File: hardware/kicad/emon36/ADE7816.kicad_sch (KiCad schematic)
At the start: 42 parts, among them J15 6_port_3.5mm_audio_jack_array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, J16 6_port_3.5mm_audio_jack_array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, U10 ADE7816

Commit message: Added lots of silkscreen info. Added silk clearance and JLCPCB stackup. Improved Dc-DC with copper pours. Added SPI testpoints.
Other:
- title: EMON36 - 36-channel single-board energy monitor -> EEMON42 - 42-channel single-board energy monitor
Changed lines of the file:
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@@
   (paper "USLetter")
   (title_block
-    (title "EMON36 - 36-channel single-board energy monitor")
+    (title "EEMON42 - 42-channel single-board energy monitor")
     (rev "1.0")
     (company "JFCInc")

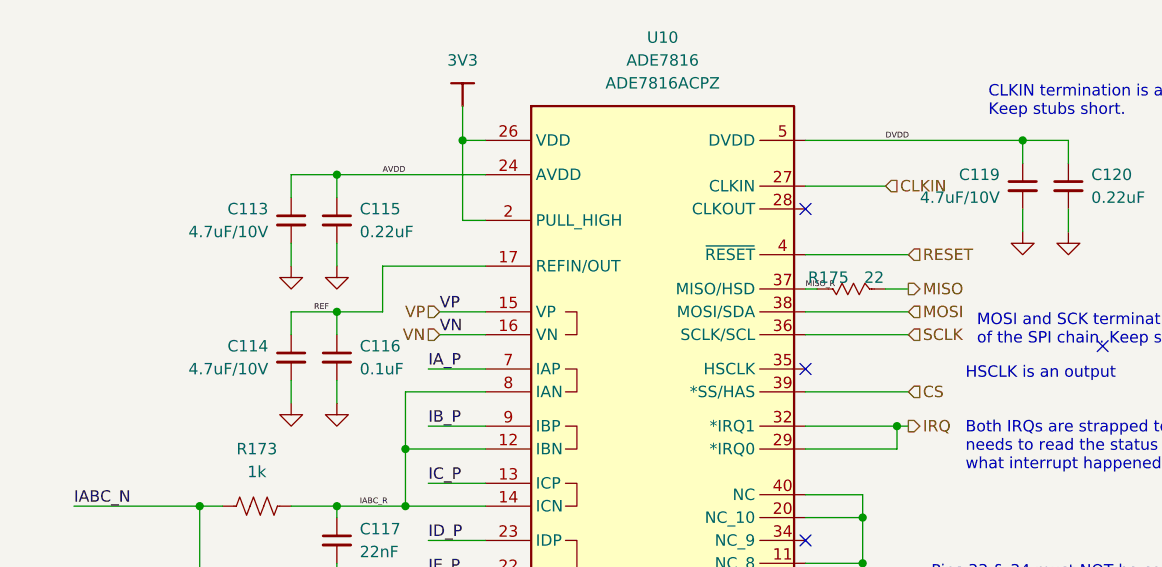
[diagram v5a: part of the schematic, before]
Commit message: Schematics: completed/updated some part number fields. Changed 4.7uF to 16V for better effective capacitance. Cleanup top sheet.
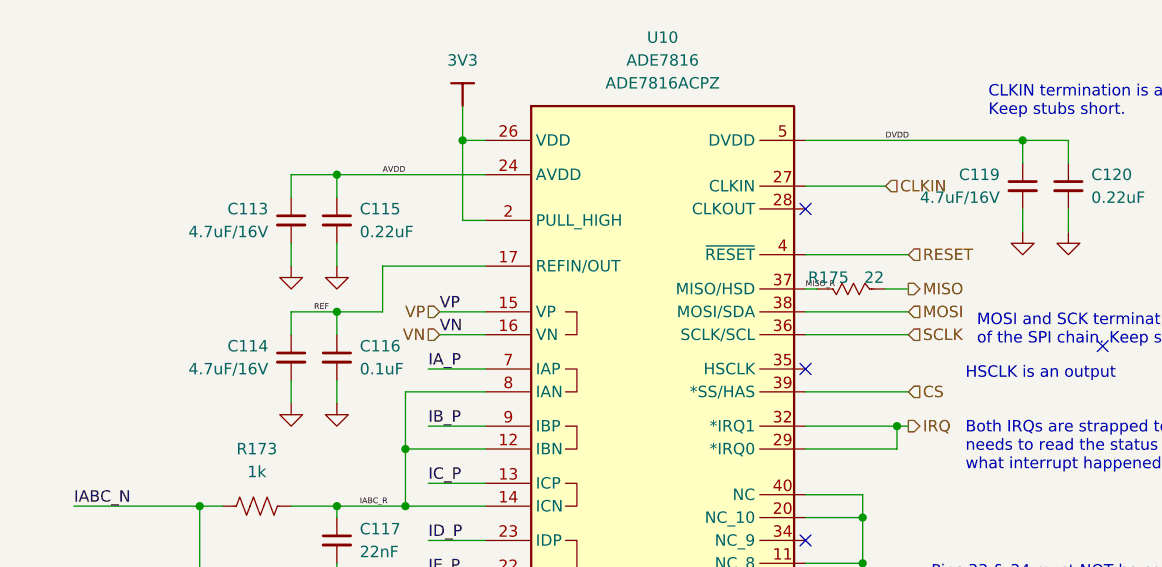
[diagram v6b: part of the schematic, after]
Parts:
- C113, C114, C119: value 4.7uF/10V -> 4.7uF/16V; Desc CAP CER 4.7UF 10V X7S 0603 -> CAP CER 4.7UF 16V X5R 0603; MFR TDK Corporation -> Samsung; MPN C1608X7S1A475K080AC -> CL10A475KO8NNNC
- U10: Desc (none) -> ENERGY MON IC 6CH QFN40
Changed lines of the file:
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@@
       (effects (font (size 1.27 1.27)) (justify right))
     )
-    (property "Value" "4.7uF/10V" (id 1) (at 135.89 64.7762 0)
+    (property "Value" "4.7uF/16V" (id 1) (at 135.89 64.7762 0)
       (effects (font (size 1.27 1.27)) (justify right))
     )
@@
       (effects (font (size 1.27 1.27)) hide)
     )
-    (property "Desc" "CAP CER 4.7UF 10V X7S 0603" (id 4) (at 138.43 63.5 0)
-      (effects (font (size 1.27 1.27)) hide)
-    )
-    (property "MFR" "TDK Corporation" (id 5) (at 138.43 63.5 0)
-      (effects (font (size 1.27 1.27)) hide)
-    )
-    (property "MPN" "C1608X7S1A475K080AC" (id 6) (at 138.43 63.5 0)
+    (property "Desc" "CAP CER 4.7UF 16V X5R 0603" (id 4) (at 138.43 63.5 0)
+      (effects (font (size 1.27 1.27)) hide)
+    )
+    (property "MFR" "Samsung" (id 5) (at 138.43 63.5 0)
+      (effects (font (size 1.27 1.27)) hide)
+    )
+    (property "MPN" "CL10A475KO8NNNC" (id 6) (at 138.43 63.5 0)
       (effects (font (size 1.27 1.27)) hide)
     )
@@
       (effects (font (size 1.27 1.27)) (justify right))
     )
-    (property "Value" "4.7uF/10V" (id 1) (at 217.17 60.9662 0)
+    (property "Value" "4.7uF/16V" (id 1) (at 217.17 60.9662 0)
       (effects (font (size 1.27 1.27)) (justify right))
     )
@@
       (effects (font (size 1.27 1.27)) hide)
     )
-    (property "Desc" "CAP CER 4.7UF 10V X7S 0603" (id 4) (at 219.71 59.69 0)
-      (effects (font (size 1.27 1.27)) hide)
-    )
-    (property "MFR" "TDK Corporation" (id 5) (at 219.71 59.69 0)
-      (effects (font (size 1.27 1.27)) hide)
-    )
-    (property "MPN" "C1608X7S1A475K080AC" (id 6) (at 219.71 59.69 0)
+    (property "Desc" "CAP CER 4.7UF 16V X5R 0603" (id 4) (at 219.71 59.69 0)
+      (effects (font (size 1.27 1.27)) hide)
+    )
+    (property "MFR" "Samsung" (id 5) (at 219.71 59.69 0)
+      (effects (font (size 1.27 1.27)) hide)
+    )
+    (property "MPN" "CL10A475KO8NNNC" (id 6) (at 219.71 59.69 0)
       (effects (font (size 1.27 1.27)) hide)
     )
@@
       (effects (font (size 1.27 1.27)) (justify right))
     )
-    (property "Value" "4.7uF/10V" (id 1) (at 135.89 80.0162 0)
+    (property "Value" "4.7uF/16V" (id 1) (at 135.89 80.0162 0)
       (effects (font (size 1.27 1.27)) (justify right))
     )
@@
       (effects (font (size 1.27 1.27)) hide)
     )
-    (property "Desc" "CAP CER 4.7UF 10V X7S 0603" (id 4) (at 138.43 78.74 0)
-      (effects (font (size 1.27 1.27)) hide)
-    )
-    (property "MFR" "TDK Corporation" (id 5) (at 138.43 78.74 0)
-      (effects (font (size 1.27 1.27)) hide)
-    )
-    (property "MPN" "C1608X7S1A475K080AC" (id 6) (at 138.43 78.74 0)
+    (property "Desc" "CAP CER 4.7UF 16V X5R 0603" (id 4) (at 138.43 78.74 0)
+      (effects (font (size 1.27 1.27)) hide)
+    )
+    (property "MFR" "Samsung" (id 5) (at 138.43 78.74 0)
+      (effects (font (size 1.27 1.27)) hide)
+    )
+    (property "MPN" "CL10A475KO8NNNC" (id 6) (at 138.43 78.74 0)
       (effects (font (size 1.27 1.27)) hide)
     )
@@
       (effects (font (size 1.27 1.27)) hide)
     )
+    (property "Desc" "ENERGY MON IC 6CH QFN40" (id 13) (at 179.07 88.9 0)
+      (effects (font (size 1.27 1.27)) hide)
+    )

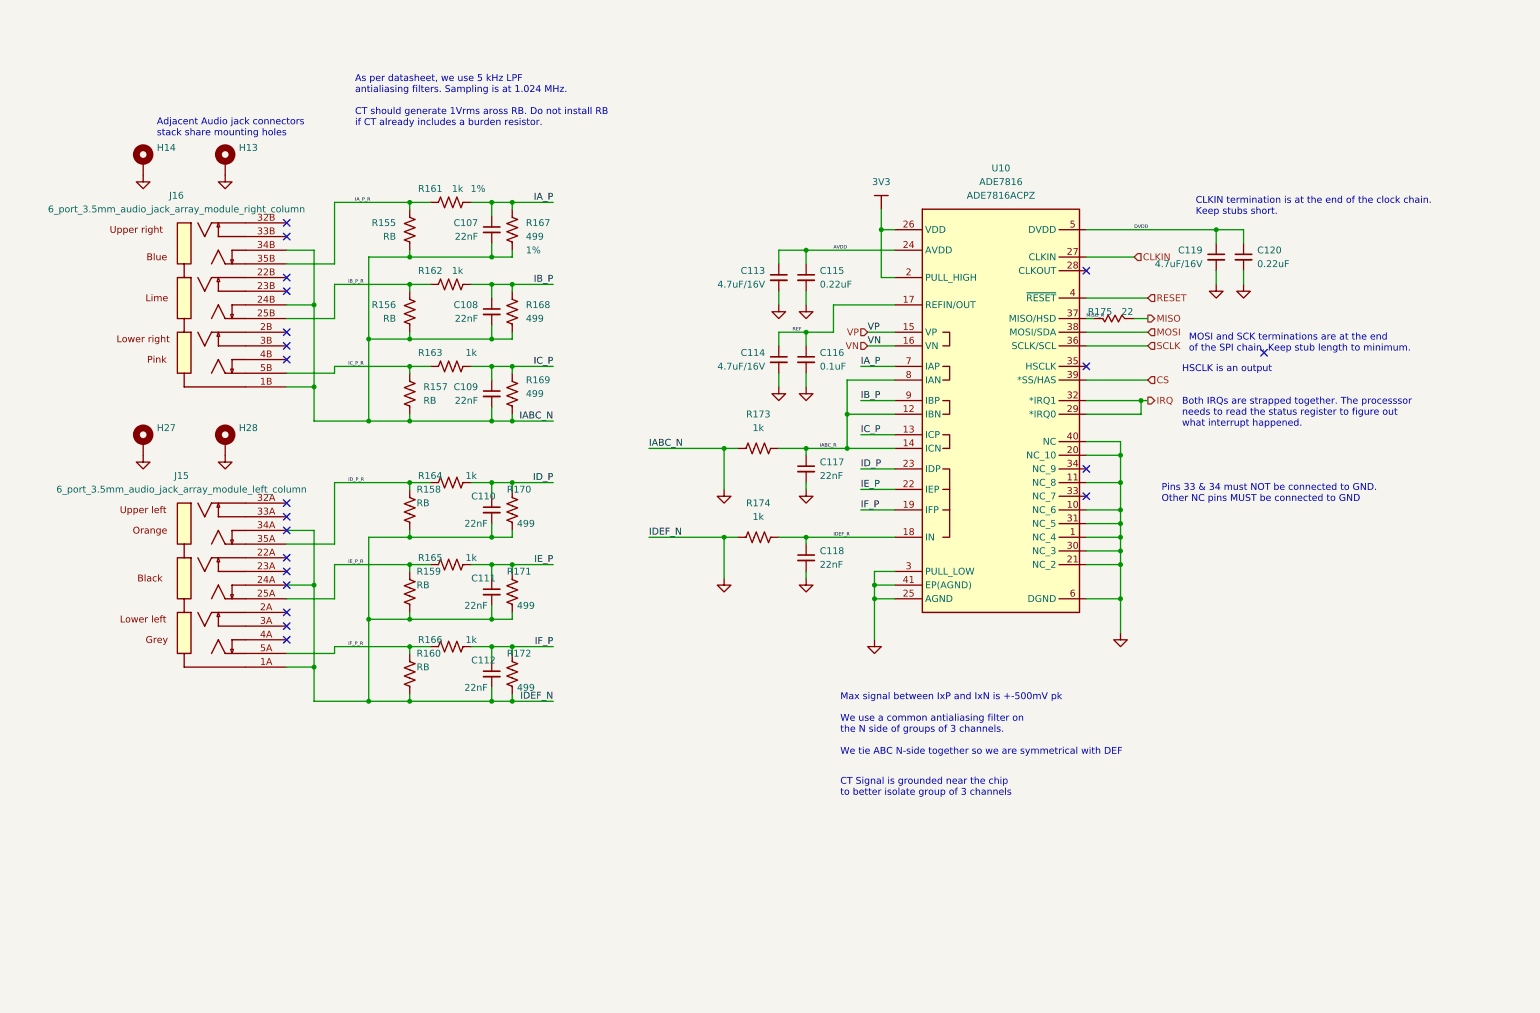
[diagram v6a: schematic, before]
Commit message: Added IRQ diodes - ADE7816 IRQs not open collector. Added pin 1 markers. Increased track widths. Cleanup. Made OLED mounting holes non plated.
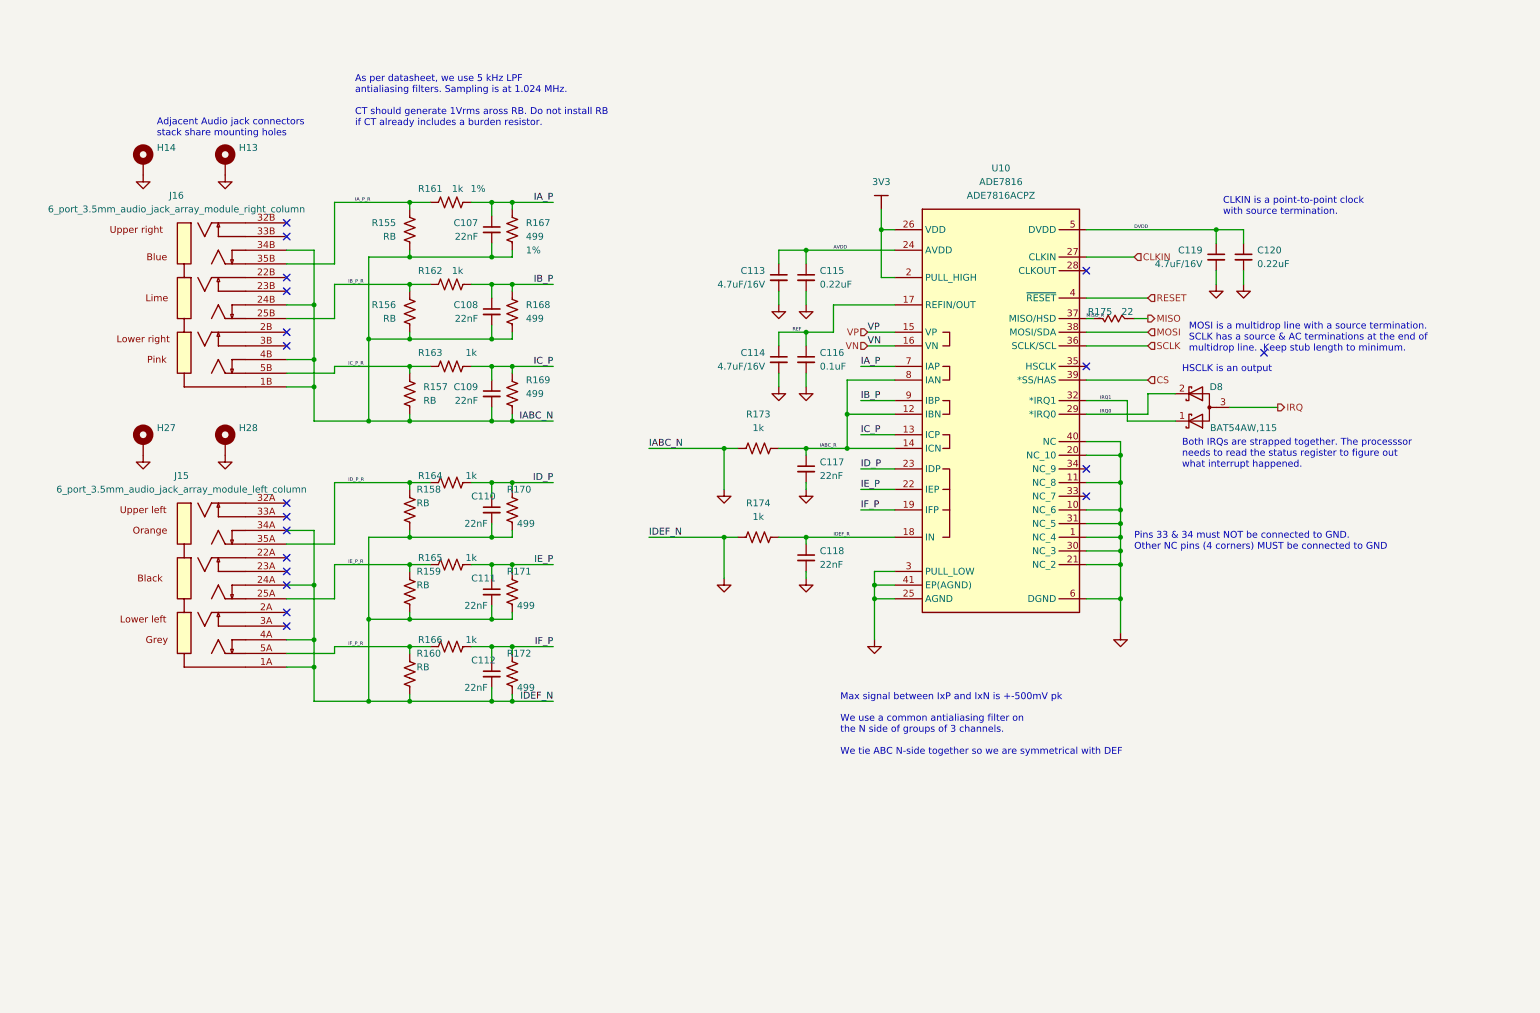
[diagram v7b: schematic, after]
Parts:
- added D8: D_Schottky_Dual_CommonAnode_KKA_Parallel, Package_TO_SOT_SMD:SOT-323_SC-70, symbol Device:D_Schottky_Dual_CommonAnode_KKA_Parallel
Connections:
- net GND: now also J15.4A, J16.4B
- net IRQ: now also D8.3 (A); no longer U10.29 (*IRQ0), U10.32 (*IRQ1)
- new net IRQ0: D8.2 (K), U10.29 (*IRQ0)
- new net IRQ1: D8.1 (K), U10.32 (*IRQ1)
- no-connect marks 21 -> 19
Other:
- note added: "CLKIN is a point-to-point clock with source termination."
- note added: "MOSI is a multidrop line with a source termination. SCLK has a source & AC terminations at the end of multidrop line. Keep stub length to minimum."
- note added: "Pins 33 & 34 must NOT be connected to GND. Other NC pins (4 corners) MUST be connected to GND"
- note removed: "CLKIN termination is at the end of the clock chain. Keep stubs short."
- note removed: "CT Signal is grounded near the chip to better isolate group of 3 channels"
- note removed: "MOSI and SCK terminations are at the end of the SPI chain. Keep stub length to minimum."
- note removed: "Pins 33 & 34 must NOT be connected to GND. Other NC pins MUST be connected to GND"
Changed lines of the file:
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@@
   (junction (at 85.09 142.24) (diameter 0) (color 0 0 0 0)
   )
-  (junction (at 205.74 86.36) (diameter 0) (color 0 0 0 0)
-  )
   (junction (at 88.9 101.6) (diameter 0) (color 0 0 0 0)
   )
@@
   (junction (at 69.85 80.01) (diameter 0) (color 0 0 0 0)
   )
+  (junction (at 52.07 130.81) (diameter 0) (color 0 0 0 0)
+  )
   (junction (at 69.85 64.77) (diameter 0) (color 0 0 0 0)
   )
@@
   )
   (junction (at 201.93 114.3) (diameter 0) (color 0 0 0 0)
+  )
+  (junction (at 52.07 78.74) (diameter 0) (color 0 0 0 0)
   )
   (junction (at 201.93 106.68) (diameter 0) (color 0 0 0 0)
@@
   (no_connect (at 46.99 66.04))
   (no_connect (at 46.99 125.73))
-  (no_connect (at 46.99 130.81))
   (no_connect (at 46.99 73.66))
   (no_connect (at 195.58 104.14))
   (no_connect (at 46.99 55.88))
   (no_connect (at 46.99 105.41))
-  (no_connect (at 46.99 78.74))
   (no_connect (at 46.99 53.34))
   (no_connect (at 195.58 62.23))
@@
     (stroke (width 0) (type default) (color 0 0 0 0))
   )
-  (wire (pts (xy 195.58 88.9) (xy 205.74 88.9))
+  (wire (pts (xy 195.58 88.9) (xy 207.01 88.9))
     (stroke (width 0) (type default) (color 0 0 0 0))
   )
@@
     (stroke (width 0) (type default) (color 0 0 0 0))
   )
-  (wire (pts (xy 52.07 120.65) (xy 52.07 135.89))
+  (wire (pts (xy 52.07 120.65) (xy 52.07 130.81))
     (stroke (width 0) (type default) (color 0 0 0 0))
   )
@@
     (stroke (width 0) (type default) (color 0 0 0 0))
   )
-  (wire (pts (xy 52.07 68.58) (xy 52.07 83.82))
+  (wire (pts (xy 52.07 68.58) (xy 52.07 78.74))
     (stroke (width 0) (type default) (color 0 0 0 0))
   )
@@
     (stroke (width 0) (type default) (color 0 0 0 0))
   )
+  (wire (pts (xy 52.07 78.74) (xy 52.07 83.82))
+    (stroke (width 0) (type default) (color 0 0 0 0))
+  )
   (wire (pts (xy 85.09 104.14) (xy 85.09 101.6))
     (stroke (width 0) (type default) (color 0 0 0 0))
@@
   )
   (wire (pts (xy 81.28 116.84) (xy 85.09 116.84))
+    (stroke (width 0) (type default) (color 0 0 0 0))
+  )
+  (wire (pts (xy 207.01 88.9) (xy 207.01 85.09))
     (stroke (width 0) (type default) (color 0 0 0 0))
   )
@@
     (stroke (width 0) (type default) (color 0 0 0 0))
   )
+  (wire (pts (xy 207.01 85.09) (xy 212.09 85.09))
+    (stroke (width 0) (type default) (color 0 0 0 0))
+  )
   (wire (pts (xy 85.09 49.53) (xy 88.9 49.53))
     (stroke (width 0) (type default) (color 0 0 0 0))
@@
     (stroke (width 0) (type default) (color 0 0 0 0))
   )
-  (wire (pts (xy 207.01 86.36) (xy 205.74 86.36))
+  (wire (pts (xy 46.99 78.74) (xy 52.07 78.74))
     (stroke (width 0) (type default) (color 0 0 0 0))
   )
@@
   )
   (wire (pts (xy 69.85 58.42) (xy 69.85 59.69))
+    (stroke (width 0) (type default) (color 0 0 0 0))
+  )
+  (wire (pts (xy 52.07 130.81) (xy 52.07 135.89))
     (stroke (width 0) (type default) (color 0 0 0 0))
   )
@@
     (stroke (width 0) (type default) (color 0 0 0 0))
   )
-  (wire (pts (xy 195.58 86.36) (xy 205.74 86.36))
+  (wire (pts (xy 231.14 87.63) (xy 222.25 87.63))
+    (stroke (width 0) (type default) (color 0 0 0 0))
+  )
+  (wire (pts (xy 195.58 86.36) (xy 203.2 86.36))
     (stroke (width 0) (type default) (color 0 0 0 0))
   )
@@
     (stroke (width 0) (type default) (color 0 0 0 0))
   )
-  (wire (pts (xy 205.74 86.36) (xy 205.74 88.9))
-    (stroke (width 0) (type default) (color 0 0 0 0))
-  )
   (wire (pts (xy 69.85 111.76) (xy 62.23 111.76))
     (stroke (width 0) (type default) (color 0 0 0 0))
@@
     (stroke (width 0) (type default) (color 0 0 0 0))
   )
+  (wire (pts (xy 203.2 86.36) (xy 203.2 90.17))
+    (stroke (width 0) (type default) (color 0 0 0 0))
+  )
   (wire (pts (xy 69.85 66.04) (xy 69.85 64.77))
     (stroke (width 0) (type default) (color 0 0 0 0))
@@
   )
   (wire (pts (xy 88.9 142.24) (xy 96.52 142.24))
+    (stroke (width 0) (type default) (color 0 0 0 0))
+  )
+  (wire (pts (xy 46.99 130.81) (xy 52.07 130.81))
     (stroke (width 0) (type default) (color 0 0 0 0))
   )
@@
     (stroke (width 0) (type default) (color 0 0 0 0))
   )
+  (wire (pts (xy 203.2 90.17) (xy 212.09 90.17))
+    (stroke (width 0) (type default) (color 0 0 0 0))
+  )
   (wire (pts (xy 156.21 120.65) (xy 160.02 120.65))
     (stroke (width 0) (type default) (color 0 0 0 0))
@@
   )
   (text "Both IRQs are strapped together. The processsor\nneeds to read the status register to figure out\nwhat interrupt happened."
-    (at 213.36 91.44 0)
+    (at 213.36 99.06 0)
     (effects (font (size 1.27 1.27)) (justify left bottom))
   )
@@
     (effects (font (size 1.27 1.27)) (justify left bottom))
   )
-  (text "MOSI and SCK terminations are at the end \nof the SPI chain. Keep stub length to minimum."
+  (text "MOSI is a multidrop line with a source termination.\nSCLK has a source & AC terminations at the end of \nmultidrop line.  Keep stub length to minimum."
     (at 214.63 77.47 0)
     (effects (font (size 1.27 1.27)) (justify left bottom))
@@
     (effects (font (size 1.27 1.27)) (justify left bottom))
   )
-  (text "CLKIN termination is at the end of the clock chain. \nKeep stubs short."
-    (at 215.9 52.07 0)
-    (effects (font (size 1.27 1.27)) (justify left bottom))
-  )
-  (text "CT Signal is grounded near the chip\nto better isolate group of 3 channels"
-    (at 149.86 160.02 0)
+  (text "CLKIN is a point-to-point clock \nwith source termination."
+    (at 220.98 52.07 0)
     (effects (font (size 1.27 1.27)) (justify left bottom))
   )
@@
     (effects (font (size 1.27 1.27)) (justify left bottom))
   )
-  (text "Pins 33 & 34 must NOT be connected to GND.\nOther NC pins MUST be connected to GND"
-    (at 209.55 105.41 0)
+  (text "Pins 33 & 34 must NOT be connected to GND.\nOther NC pins (4 corners) MUST be connected to GND"
+    (at 204.47 114.3 0)
     (effects (font (size 1.27 1.27)) (justify left bottom))
   )
@@
     (effects (font (size 1.27 1.27)) (justify right bottom))
   )
+  (label "IRQ0" (at 198.12 88.9 0)
+    (effects (font (size 0.635 0.635)) (justify left bottom))
+  )
   (label "IABC_N" (at 114.3 95.25 0)
     (effects (font (size 1.27 1.27)) (justify left bottom))
+  )
+  (label "IRQ1" (at 198.12 86.36 0)
+    (effects (font (size 0.635 0.635)) (justify left bottom))
   )
   (label "IF_P_R" (at 58.42 132.08 0)
@@
     (effects (font (size 1.27 1.27)) (justify left))
   )
-  (hierarchical_label "IRQ" (shape output) (at 207.01 86.36 0)
+  (hierarchical_label "IRQ" (shape output) (at 231.14 87.63 0)
     (effects (font (size 1.27 1.27)) (justify left))
   )
@@
     (pin "2")
   )
+  (symbol (lib_id "Device:D_Schottky_Dual_CommonAnode_KKA_Parallel") (at 217.17 87.63 180) (unit 1)
+    (in_bom yes) (on_board yes)
+    (property "Reference" "D8" (id 0) (at 219.71 83.82 0))
+    (property "Value" "D_Schottky_Dual_CommonAnode_KKA_Parallel" (id 1) (at 216.8525 81.28 0)
+      (effects (font (size 1.27 1.27)) hide)
+    )
+    (property "Footprint" "Package_TO_SOT_SMD:SOT-323_SC-70" (id 2) (at 218.44 87.63 0)
+      (effects (font (size 1.27 1.27)) hide)
+    )
+    (property "Datasheet" "~" (id 3) (at 218.44 87.63 0)
+      (effects (font (size 1.27 1.27)) hide)
+    )
+    (property "MFR" "Nexperia" (id 4) (at 217.17 87.63 0)
+      (effects (font (size 1.27 1.27)) hide)
+    )
+    (property "MPN" "BAT54AW,115" (id 5) (at 224.79 91.44 0))
+    (pin "1")
+    (pin "2")
+    (pin "3")
+  )
   (symbol (lib_id "power:GND") (at 20.32 96.52 0) (unit 1)
